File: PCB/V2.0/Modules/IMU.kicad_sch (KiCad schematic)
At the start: 2 parts, among them J40 Conn_01x08_Socket, J7 VIRTUAL_MPU6050

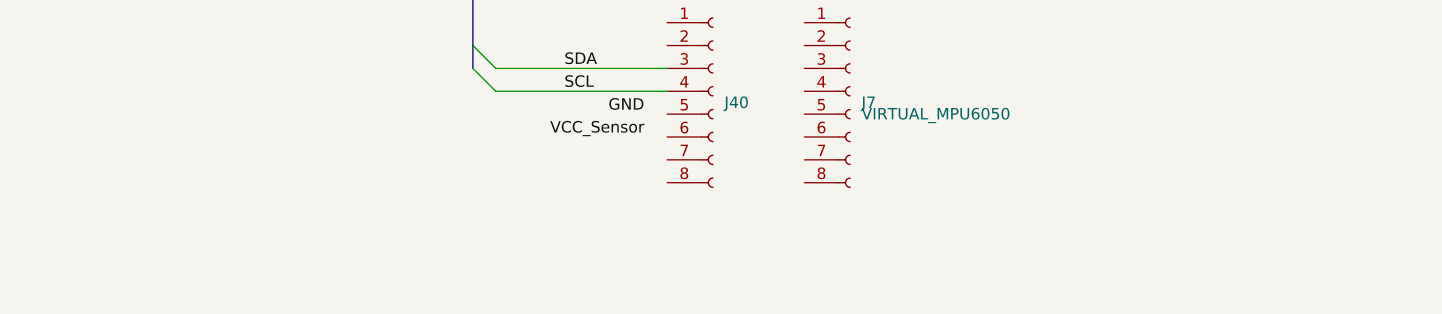
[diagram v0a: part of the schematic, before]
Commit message: Update V2.0 form factor
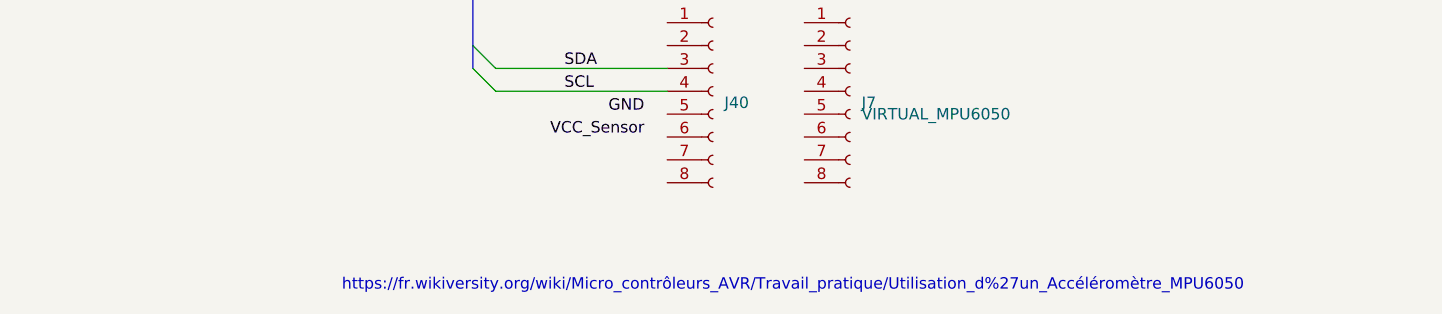
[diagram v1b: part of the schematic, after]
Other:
- note added: "https://fr.wikiversity.org/wiki/Micro_contrôleurs_AVR/Travail_pratique/Utilisation_d%27un_Accéléromètre_MPU6050"
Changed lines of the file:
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@@
+		)
+	)
+	(text "https://fr.wikiversity.org/wiki/Micro_contrôleurs_AVR/Travail_pratique/Utilisation_d%27un_Accéléromètre_MPU6050"
+		(exclude_from_sim no)
+		(at 133.35 95.25 0)
+		(effects
+			(font
+				(size 1.27 1.27)
+			)
 		)
 	)

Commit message: Update board
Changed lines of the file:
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@@
-		)
-	)
-	(wire
-		(pts
-			(xy 25.4 31.75) (xy 30.48 31.75)
-		)
-		(stroke
-			(width 0)
-			(type default)
 		)
 	)
@@
 		)
 	)
-	(label "+5V"
-		(at 25.4 31.75 180)
-		(fields_autoplaced yes)
-		(effects
-			(font
-				(size 1.27 1.27)
-			)
-			(justify right bottom)
-		)
-	)
 	(label "GND"
 		(at 116.84 76.2 180)
-		(fields_autoplaced yes)
 		(effects
 			(font
@@
 	(label "GND"
 		(at 26.67 25.4 180)
-		(fields_autoplaced yes)
 		(effects
 			(font
@@
 	(label "SCL"
 		(at 107.95 73.66 0)
-		(fields_autoplaced yes)
 		(effects
 			(font
@@
 	(label "SDA"
 		(at 107.95 71.12 0)
-		(fields_autoplaced yes)
 		(effects
 			(font
@@
 	(label "+3.3V"
 		(at 26.67 29.21 180)
-		(fields_autoplaced yes)
 		(effects
 			(font
@@
 	(label "VCC_Sensor"
 		(at 116.84 78.74 180)
-		(fields_autoplaced yes)
 		(effects
 			(font
@@
 		)
 	)
-	(hierarchical_label "{I2C}"
-		(shape input)
+	(hierarchical_label "{I2C0}"
+		(shape bidirectional)
 		(at 95.25 59.69 180)
-		(fields_autoplaced yes)
 		(effects
 			(font
@@
 		)
 	)
-	(hierarchical_label "+5V"
-		(shape input)
-		(at 30.48 31.75 0)
-		(fields_autoplaced yes)
-		(effects
-			(font
-				(size 1.27 1.27)
-			)
-			(justify left)
-		)
-	)
 	(hierarchical_label "GND"
 		(shape passive)
 		(at 30.48 25.4 0)
-		(fields_autoplaced yes)
 		(effects
 			(font
@@
 		(shape input)
 		(at 30.48 29.21 0)
-		(fields_autoplaced yes)
 		(effects
 			(font
